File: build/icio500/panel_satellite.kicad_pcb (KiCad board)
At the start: 2 copper layers, 38.1 x 133.3 mm, 30 parts, among them J1 SM08B-SRSS-TB, U1 IS31FL3236

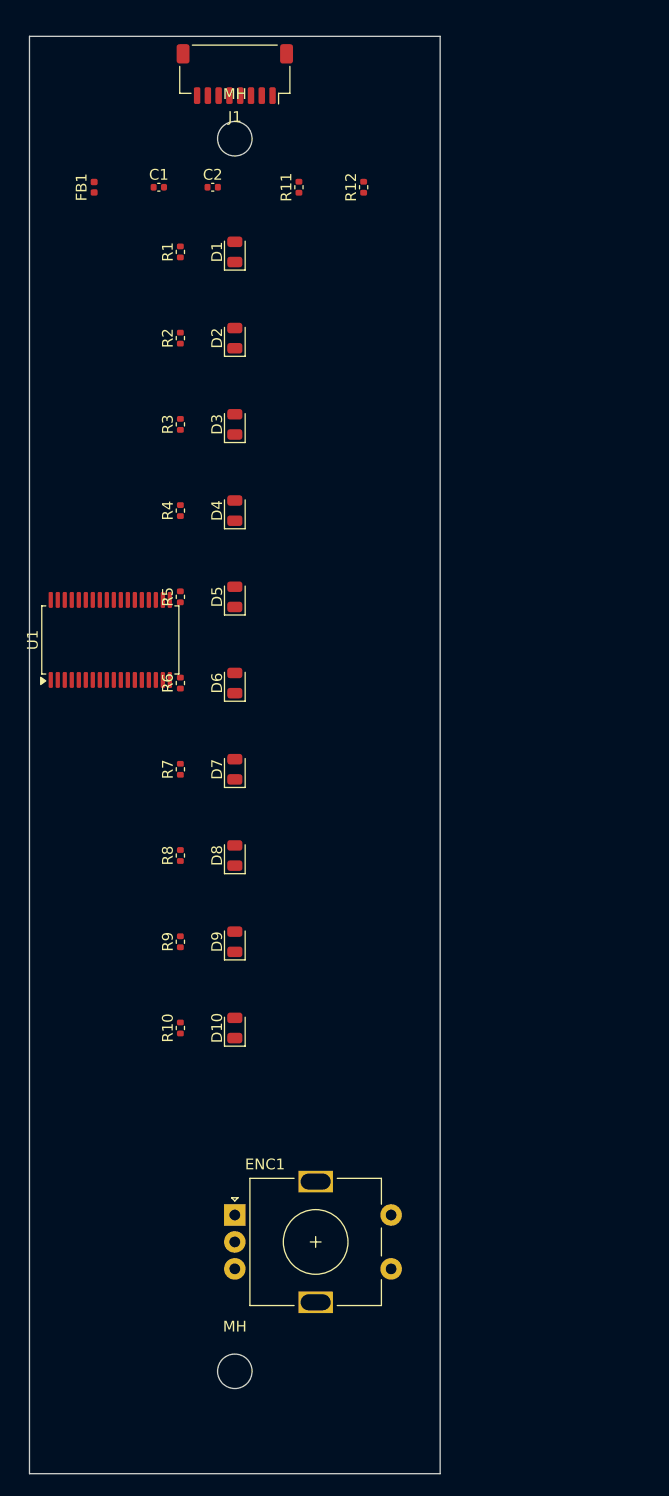
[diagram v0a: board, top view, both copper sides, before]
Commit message: Clean up repo, add mounting holes to faceplate for mating, and assign nets/zones on satellite board via python
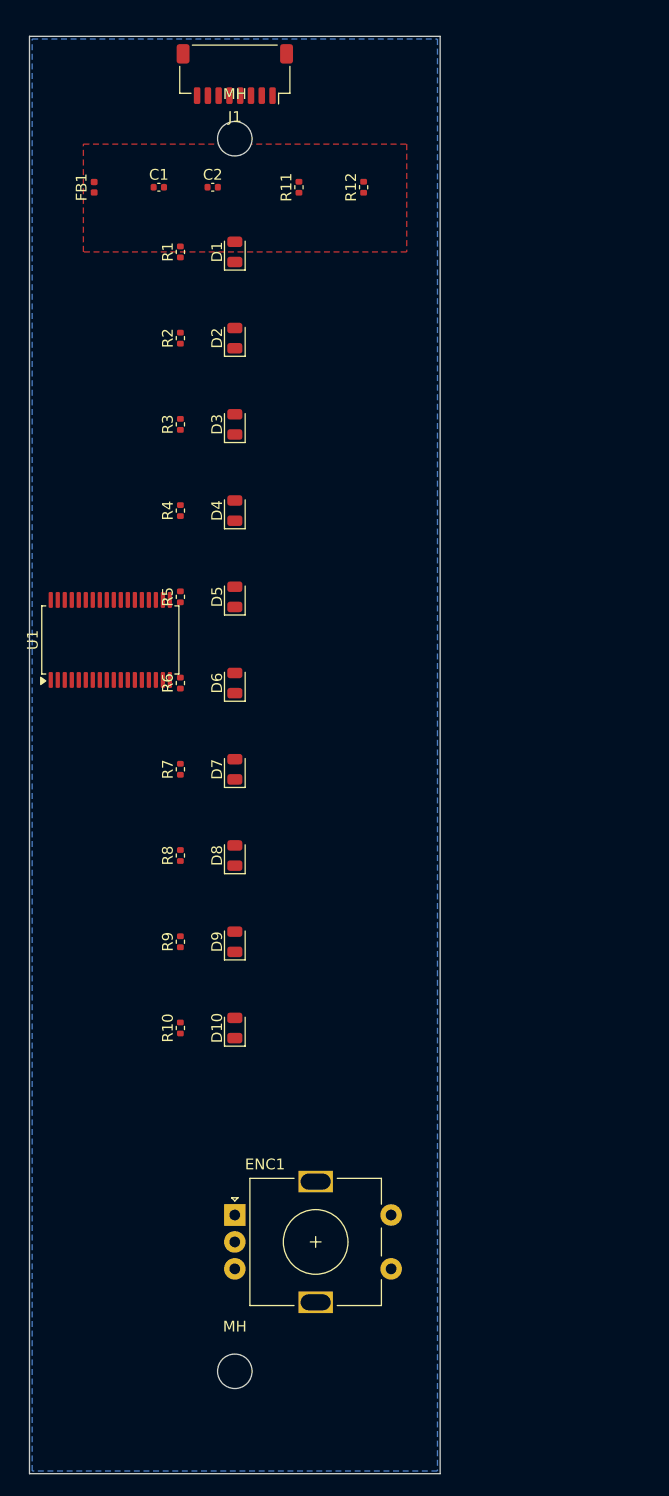
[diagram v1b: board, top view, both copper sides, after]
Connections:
- C1 pad 1: (no net) -> +3V3_CLEAN
- C1 pad 2: (no net) -> GND
- C2 pad 1: (no net) -> +3V3_CLEAN
- C2 pad 2: (no net) -> GND
- FB1 pad 1: (no net) -> +3V3
- FB1 pad 2: (no net) -> +3V3_CLEAN
- J1 pad 1: (no net) -> +3V3
- J1 pad 2: (no net) -> GND
- J1 pad 3: (no net) -> SDA
- J1 pad 4: (no net) -> SCL
- J1 pad 5: (no net) -> ENC_A
- J1 pad 6: (no net) -> ENC_B
- J1 pad 7: (no net) -> ENC_SW
- J1 pad 8: (no net) -> GND
- R1 pad 1: (no net) -> LED_1
- R1 pad 2: (no net) -> LED_1_A
- R10 pad 1: (no net) -> LED_10
- R10 pad 2: (no net) -> LED_10_A
- R11 pad 1: (no net) -> +3V3_CLEAN
- R11 pad 2: (no net) -> SDA
- R12 pad 1: (no net) -> +3V3_CLEAN
- R12 pad 2: (no net) -> SCL
- R2 pad 1: (no net) -> LED_2
- R2 pad 2: (no net) -> LED_2_A
- R3 pad 1: (no net) -> LED_3
- R3 pad 2: (no net) -> LED_3_A
- R4 pad 1: (no net) -> LED_4
- R4 pad 2: (no net) -> LED_4_A
- R5 pad 1: (no net) -> LED_5
- R5 pad 2: (no net) -> LED_5_A
- R6 pad 1: (no net) -> LED_6
- R6 pad 2: (no net) -> LED_6_A
- R7 pad 1: (no net) -> LED_7
- R7 pad 2: (no net) -> LED_7_A
- R8 pad 1: (no net) -> LED_8
- R8 pad 2: (no net) -> LED_8_A
- R9 pad 1: (no net) -> LED_9
- R9 pad 2: (no net) -> LED_9_A
- U1 pad 1: (no net) -> LED_9
- U1 pad 10: (no net) -> GND
- U1 pad 11: (no net) -> SCL
- U1 pad 12: (no net) -> SDA
- U1 pad 13: (no net) -> +3V3_CLEAN
- U1 pad 14: (no net) -> GND
- U1 pad 15: (no net) -> +3V3_CLEAN
- U1 pad 16: (no net) -> +3V3_CLEAN
- U1 pad 17: (no net) -> GND
- U1 pad 18: (no net) -> GND
- U1 pad 19: (no net) -> LED_10
- U1 pad 2: (no net) -> LED_8
- U1 pad 3: (no net) -> LED_7
- U1 pad 4: (no net) -> LED_6
- U1 pad 5: (no net) -> LED_5
- U1 pad 6: (no net) -> LED_4
- U1 pad 7: (no net) -> LED_3
- U1 pad 8: (no net) -> LED_2
- U1 pad 9: (no net) -> LED_1
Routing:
- added copper zone on F.Cu, net +3V3_CLEAN
- added copper zone on B.Cu, net GND
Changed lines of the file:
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@@
 			(layers "F.Cu" "F.Mask" "F.Paste")
 			(roundrect_rratio 0.25)
+			(net "LED_3")
 		)
 		(pad "2" smd roundrect
@@
 			(layers "F.Cu" "F.Mask" "F.Paste")
 			(roundrect_rratio 0.25)
+			(net "LED_3_A")
 		)
 		(embedded_fonts no)
@@
 			(layers "F.Cu" "F.Mask" "F.Paste")
 			(roundrect_rratio 0.25)
+			(net "LED_10")
 		)
 		(pad "2" smd roundrect
@@
 			(layers "F.Cu" "F.Mask" "F.Paste")
 			(roundrect_rratio 0.25)
+			(net "LED_10_A")
 		)
 		(embedded_fonts no)
@@
 			(layers "F.Cu" "F.Mask" "F.Paste")
 			(roundrect_rratio 0.25)
+			(net "+3V3_CLEAN")
 		)
 		(pad "2" smd roundrect
@@
 			(layers "F.Cu" "F.Mask" "F.Paste")
 			(roundrect_rratio 0.25)
+			(net "SCL")
 		)
 		(embedded_fonts no)
@@
 			(layers "F.Cu" "F.Mask" "F.Paste")
 			(roundrect_rratio 0.25)
+			(net "LED_2")
 		)
 		(pad "2" smd roundrect
@@
 			(layers "F.Cu" "F.Mask" "F.Paste")
 			(roundrect_rratio 0.25)
+			(net "LED_2_A")
 		)
 		(embedded_fonts no)
@@
 			(layers "F.Cu" "F.Mask" "F.Paste")
 			(roundrect_rratio 0.25)
+			(net "+3V3")
 		)
 		(pad "2" smd roundrect
@@
 			(layers "F.Cu" "F.Mask" "F.Paste")
 			(roundrect_rratio 0.25)
+			(net "GND")
 		)
 		(pad "3" smd roundrect
@@
 			(layers "F.Cu" "F.Mask" "F.Paste")
 			(roundrect_rratio 0.25)
+			(net "SDA")
 		)
 		(pad "4" smd roundrect
@@
 			(layers "F.Cu" "F.Mask" "F.Paste")
 			(roundrect_rratio 0.25)
+			(net "SCL")
 		)
 		(pad "5" smd roundrect
@@
 			(layers "F.Cu" "F.Mask" "F.Paste")
 			(roundrect_rratio 0.25)
+			(net "ENC_A")
 		)
 		(pad "6" smd roundrect
@@
 			(layers "F.Cu" "F.Mask" "F.Paste")
 			(roundrect_rratio 0.25)
+			(net "ENC_B")
 		)
 		(pad "7" smd roundrect
@@
 			(layers "F.Cu" "F.Mask" "F.Paste")
 			(roundrect_rratio 0.25)
+			(net "ENC_SW")
 		)
 		(pad "8" smd roundrect
@@
 			(layers "F.Cu" "F.Mask" "F.Paste")
 			(roundrect_rratio 0.25)
+			(net "GND")
 		)
 		(pad "MP" smd roundrect
@@
 			(layers "F.Cu" "F.Mask" "F.Paste")
 			(roundrect_rratio 0.25)
+			(net "+3V3_CLEAN")
 		)
 		(pad "2" smd roundrect
@@
 			(layers "F.Cu" "F.Mask" "F.Paste")
 			(roundrect_rratio 0.25)
+			(net "GND")
 		)
 		(embedded_fonts no)
@@
 			(layers "F.Cu" "F.Mask" "F.Paste")
 			(roundrect_rratio 0.25)
+			(net "LED_1")
 		)
 		(pad "2" smd roundrect
@@
 			(layers "F.Cu" "F.Mask" "F.Paste")
 			(roundrect_rratio 0.25)
+			(net "LED_1_A")
 		)
 		(embedded_fonts no)
@@
 			(layers "F.Cu" "F.Mask" "F.Paste")
 			(roundrect_rratio 0.25)
+			(net "LED_9")
 		)
 		(pad "2" smd roundrect
@@
 			(layers "F.Cu" "F.Mask" "F.Paste")
 			(roundrect_rratio 0.25)
+			(net "LED_8")
 		)
 		(pad "3" smd roundrect
@@
 			(layers "F.Cu" "F.Mask" "F.Paste")
 			(roundrect_rratio 0.25)
+			(net "LED_7")
 		)
 		(pad "4" smd roundrect
@@
 			(layers "F.Cu" "F.Mask" "F.Paste")
 			(roundrect_rratio 0.25)
+			(net "LED_6")
 		)
 		(pad "5" smd roundrect
@@
 			(layers "F.Cu" "F.Mask" "F.Paste")
 			(roundrect_rratio 0.25)
+			(net "LED_5")
 		)
 		(pad "6" smd roundrect
@@
 			(layers "F.Cu" "F.Mask" "F.Paste")
 			(roundrect_rratio 0.25)
+			(net "LED_4")
 		)
 		(pad "7" smd roundrect
@@
 			(layers "F.Cu" "F.Mask" "F.Paste")
 			(roundrect_rratio 0.25)
+			(net "LED_3")
 		)
 		(pad "8" smd roundrect
@@
 			(layers "F.Cu" "F.Mask" "F.Paste")
 			(roundrect_rratio 0.25)
+			(net "LED_2")
 		)
 		(pad "9" smd roundrect
@@
 			(layers "F.Cu" "F.Mask" "F.Paste")
 			(roundrect_rratio 0.25)
+			(net "LED_1")
 		)
 		(pad "10" smd roundrect
@@
 			(layers "F.Cu" "F.Mask" "F.Paste")
 			(roundrect_rratio 0.25)
+			(net "GND")
 		)
 		(pad "11" smd roundrect
@@
 			(layers "F.Cu" "F.Mask" "F.Paste")
 			(roundrect_rratio 0.25)
+			(net "SCL")
 		)
 		(pad "12" smd roundrect
@@
 			(layers "F.Cu" "F.Mask" "F.Paste")
 			(roundrect_rratio 0.25)
+			(net "SDA")
 		)
 		(pad "13" smd roundrect
@@
 			(layers "F.Cu" "F.Mask" "F.Paste")
 			(roundrect_rratio 0.25)
+			(net "+3V3_CLEAN")
 		)
 		(pad "14" smd roundrect
@@
 			(layers "F.Cu" "F.Mask" "F.Paste")
 			(roundrect_rratio 0.25)
+			(net "GND")
 		)
 		(pad "15" smd roundrect
@@
 			(layers "F.Cu" "F.Mask" "F.Paste")
 			(roundrect_rratio 0.25)
+			(net "+3V3_CLEAN")
 		)
 		(pad "16" smd roundrect
@@
 			(layers "F.Cu" "F.Mask" "F.Paste")
 			(roundrect_rratio 0.25)
+			(net "+3V3_CLEAN")
 		)
 		(pad "17" smd roundrect
@@
 			(layers "F.Cu" "F.Mask" "F.Paste")
 			(roundrect_rratio 0.25)
+			(net "GND")
 		)
 		(pad "18" smd roundrect
@@
 			(layers "F.Cu" "F.Mask" "F.Paste")
 			(roundrect_rratio 0.25)
+			(net "GND")
 		)
 		(pad "19" smd roundrect
@@
 			(layers "F.Cu" "F.Mask" "F.Paste")
 			(roundrect_rratio 0.25)
+			(net "LED_10")
 		)
 		(pad "20" smd roundrect
@@
 			(layers "F.Cu" "F.Mask" "F.Paste")
 			(roundrect_rratio 0.25)
+			(net "+3V3_CLEAN")
 		)
 		(pad "2" smd roundrect
@@
 			(layers "F.Cu" "F.Mask" "F.Paste")
 			(roundrect_rratio 0.25)
+			(net "GND")
 		)
 		(embedded_fonts no)
@@
 			(layers "F.Cu" "F.Mask" "F.Paste")
 			(roundrect_rratio 0.25)
+			(net "LED_9")
 		)
 		(pad "2" smd roundrect
@@
 			(layers "F.Cu" "F.Mask" "F.Paste")
 			(roundrect_rratio 0.25)
+			(net "LED_9_A")
 		)
 		(embedded_fonts no)
@@
 			(layers "F.Cu" "F.Mask" "F.Paste")
 			(roundrect_rratio 0.25)
+			(net "+3V3")
 		)
 		(pad "2" smd roundrect
@@
 			(layers "F.Cu" "F.Mask" "F.Paste")
 			(roundrect_rratio 0.25)
+			(net "+3V3_CLEAN")
 		)
 		(embedded_fonts no)
@@
 			(layers "F.Cu" "F.Mask" "F.Paste")
 			(roundrect_rratio 0.25)
+			(net "LED_5")
 		)
 		(pad "2" smd roundrect
@@
 			(layers "F.Cu" "F.Mask" "F.Paste")
 			(roundrect_rratio 0.25)
+			(net "LED_5_A")
 		)
 		(embedded_fonts no)
@@
 			(layers "F.Cu" "F.Mask" "F.Paste")
 			(roundrect_rratio 0.25)
+			(net "LED_8")
 		)
 		(pad "2" smd roundrect
@@
 			(layers "F.Cu" "F.Mask" "F.Paste")
 			(roundrect_rratio 0.25)
+			(net "LED_8_A")
 		)
 		(embedded_fonts no)
@@
 			(layers "F.Cu" "F.Mask" "F.Paste")
 			(roundrect_rratio 0.25)
+			(net "LED_4")
 		)
 		(pad "2" smd roundrect
@@
 			(layers "F.Cu" "F.Mask" "F.Paste")
 			(roundrect_rratio 0.25)
+			(net "LED_4_A")
 		)
 		(embedded_fonts no)
@@
 			(layers "F.Cu" "F.Mask" "F.Paste")
 			(roundrect_rratio 0.25)
+			(net "+3V3_CLEAN")
 		)
 		(pad "2" smd roundrect
@@
 			(layers "F.Cu" "F.Mask" "F.Paste")
 			(roundrect_rratio 0.25)
+			(net "SDA")
 		)
 		(embedded_fonts no)
@@
 			(layers "F.Cu" "F.Mask" "F.Paste")
 			(roundrect_rratio 0.25)
+			(net "LED_6")
 		)
 		(pad "2" smd roundrect
@@
 			(layers "F.Cu" "F.Mask" "F.Paste")
 			(roundrect_rratio 0.25)
+			(net "LED_6_A")
 		)
 		(embedded_fonts no)
@@
 			(layers "F.Cu" "F.Mask" "F.Paste")
 			(roundrect_rratio 0.25)
+			(net "LED_7")
 		)
 		(pad "2" smd roundrect
@@
 			(layers "F.Cu" "F.Mask" "F.Paste")
 			(roundrect_rratio 0.25)
+			(net "LED_7_A")
 		)
 		(embedded_fonts no)
@@
 		(layer "Edge.Cuts")
 	)
+	(zone
+		(net "+3V3_CLEAN")
+		(layer "F.Cu")
+		(hatch edge 0.5)
+		(connect_pads
+			(clearance 0.5)
+		)
+		(min_thickness 0.25)
+		(fill yes
+			(thermal_gap 0.5)
+			(thermal_bridge_width 0.5)
+			(island_removal_mode 0)
+		)
+		(polygon
+			(pts
+				(xy 105 110) (xy 135 110) (xy 135 120) (xy 105 120)
+			)
+		)
+	)
+	(zone
+		(net "GND")
+		(layer "B.Cu")
+		(hatch edge 0.5)
+		(connect_pads
+			(clearance 0.5)
+		)
+		(min_thickness 0.25)
+		(fill yes
+			(thermal_gap 0.5)
+			(thermal_bridge_width 0.5)
+			(island_removal_mode 0)
+		)
+		(polygon
+			(pts
+				(xy 100.25 100.25) (xy 137.85 100.25) (xy 137.85 233.1) (xy 100.25 233.1)
+			)
+		)
+	)
 	(embedded_fonts no)

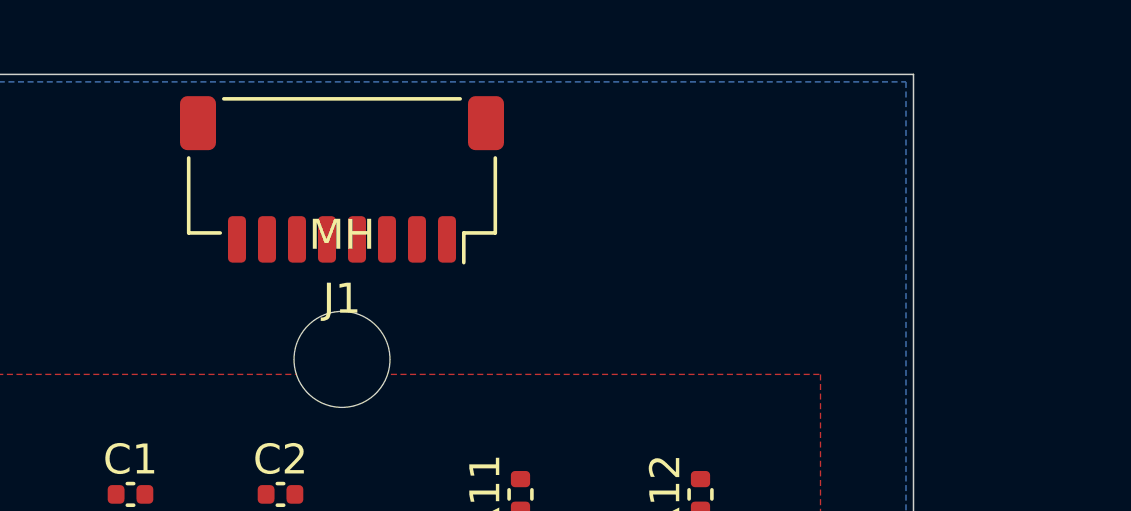
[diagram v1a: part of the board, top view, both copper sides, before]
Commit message: Integration: Sync faceplate connector to main board pinout
- Replaced the incorrect 8-pin JST-SH connector on the satellite logic board with the correct 20-pin vertical pin header (PinHeader_2x10_P2.54mm_Vertical).
- This syncs the physical layout of the faceplate interconnect back to the original schematic design in faceplate.ato, which uses a 20-pin ribbon cable with interleaved ground guard channels between the sensitive digital I2C and capacitive touch lines.
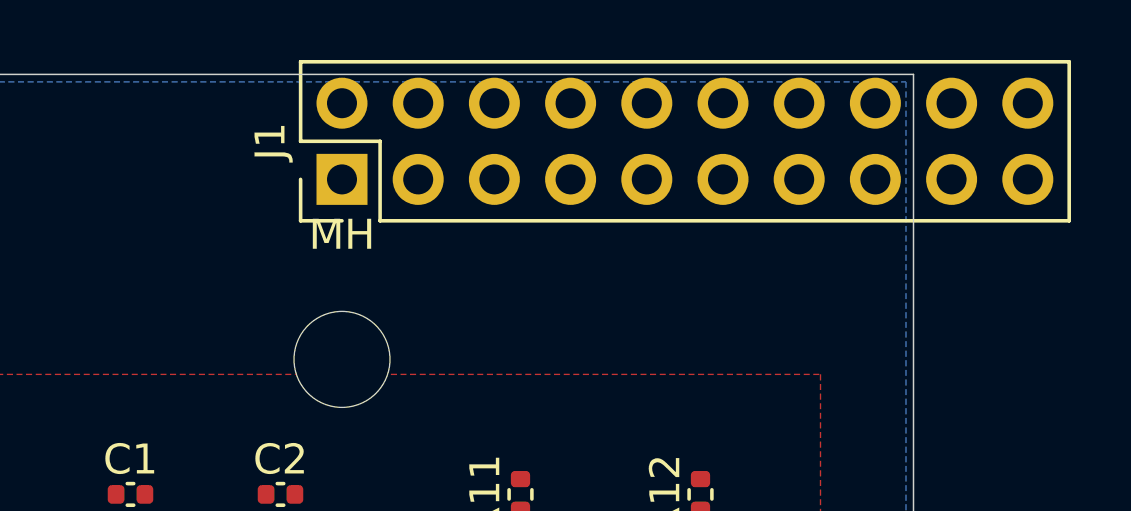
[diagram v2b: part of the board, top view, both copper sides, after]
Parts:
- J1: value SM08B-SRSS-TB -> ?; footprint JST_SH_SM08B-SRSS-TB_1x08-1MP_P1.00mm_Horizontal -> Connector_PinHeader_2.54mm:PinHeader_2x10_P2.54mm_Vertical
- turned J1 to 90 degrees
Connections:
- net ENC_B renamed i2c1_scl
- J1 pad 1: +3V3 -> daisy_5v_power
- J1 pad 2: GND -> audio_in_r
- J1 pad 3: SDA -> gnd
- J1 pad 4: SCL -> i2c1_sda
- J1 pad 5: ENC_A -> gnd
- J1 pad 7: ENC_SW -> gnd
- J1 pad 8: GND -> d13
